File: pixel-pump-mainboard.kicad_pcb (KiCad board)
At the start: 4 copper layers, 68 x 67.3 mm, 130 parts, among them J1 JST NC Valve, J10 BM10B-SRSS-TB(LF)(SN), J11 UART/SWD DNP, J12 TYPE-C-31-M-12, J2 JST NO Valve, J3 6P4C, J4 JST 3 Way Valve, J5 Jack-DC 12V, J6 Power Sw, J7 EXP1, J8 EXP2, J9 BM04B-SRSS-TBT(LF)(SN), Q1 BSS138, Q2 BSS138, Q3 BSS138, Q4 STN4NF20L, Q5 BSS138, SW1 BOOTSEL, U1 LD1117S33TR, U2 TPS62112RSAR, U3 W25Q128JVS, U4 RP2040, Y1 ABMM2-12.000MHZ-E2-T

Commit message: Add robins logo
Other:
- board text added: "REV 7"
- board text removed: "Rev 7"
- board text removed: "by Robin Reiter Hergatz, DE Aug 2022"

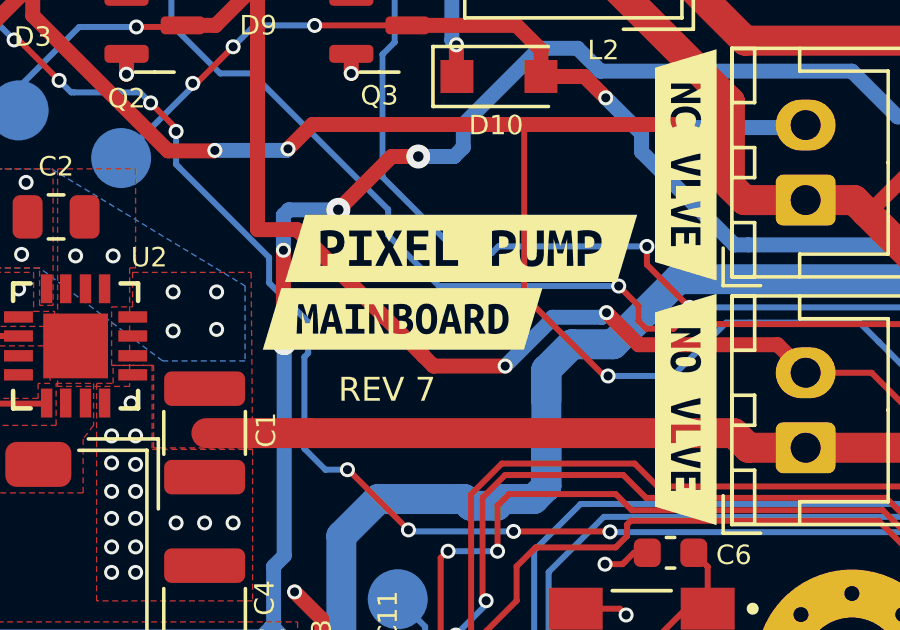
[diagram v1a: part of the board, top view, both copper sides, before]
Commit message: Change appearance of labels
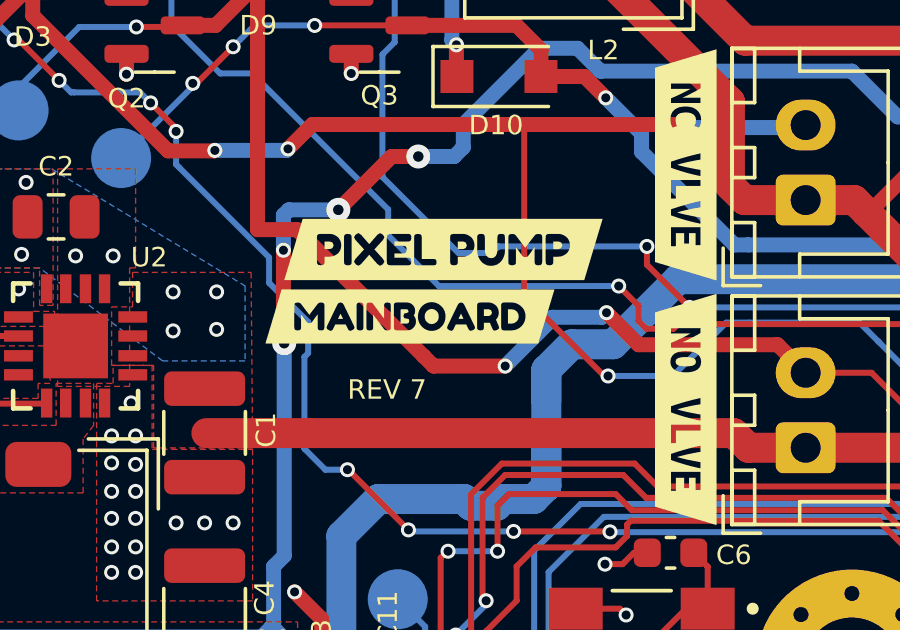
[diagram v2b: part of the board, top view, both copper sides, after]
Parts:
- removed kibuzzard-61080AF0: G***, kibuzzard-61080AF0
- removed kibuzzard-61080B06: G***, kibuzzard-61080B06
- added kibuzzard-62EBC211: G***, kibuzzard-62EBC211, F.Cu at (85.3, 115.6)
- added kibuzzard-62EBC230: G***, kibuzzard-62EBC230, F.Cu at (86.5, 113.4)

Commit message: Change appearance of labels (again)
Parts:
- moved kibuzzard-62EBC211 0.18 mm to (85.5, 115.5)
- moved kibuzzard-62EBC230 0.18 mm to (86.6, 113.3)
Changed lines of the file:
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@@
   )
   (footprint "kibuzzard-62EBC230" (layer "F.Cu")
-    (at 86.4616 113.3856)
+    (at 86.614 113.284)
     (descr "Converted using: scripting")
     (tags "svg2mod")
@@
   )
   (footprint "kibuzzard-62EBC211" (layer "F.Cu")
-    (at 85.344 115.6208)
+    (at 85.4964 115.5192)
     (descr "Converted using: scripting")
     (tags "svg2mod")
@@
   (gr_arc (start 129.699998 139.450136) (mid 130.567849 136.355905) (end 132.918238 134.164307) (layer "Edge.Cuts") (width 0.2))
   (gr_line (start 70.5 139.450136) (end 70.5 152.434856) (layer "Edge.Cuts") (width 0.2))
-  (gr_text "REV 7" (at 84.582 118.0592) (layer "F.SilkS")
+  (gr_text "REV 7" (at 84.8868 117.4496) (layer "F.SilkS")
     (effects (font (size 0.65 0.65) (thickness 0.13)))
   )

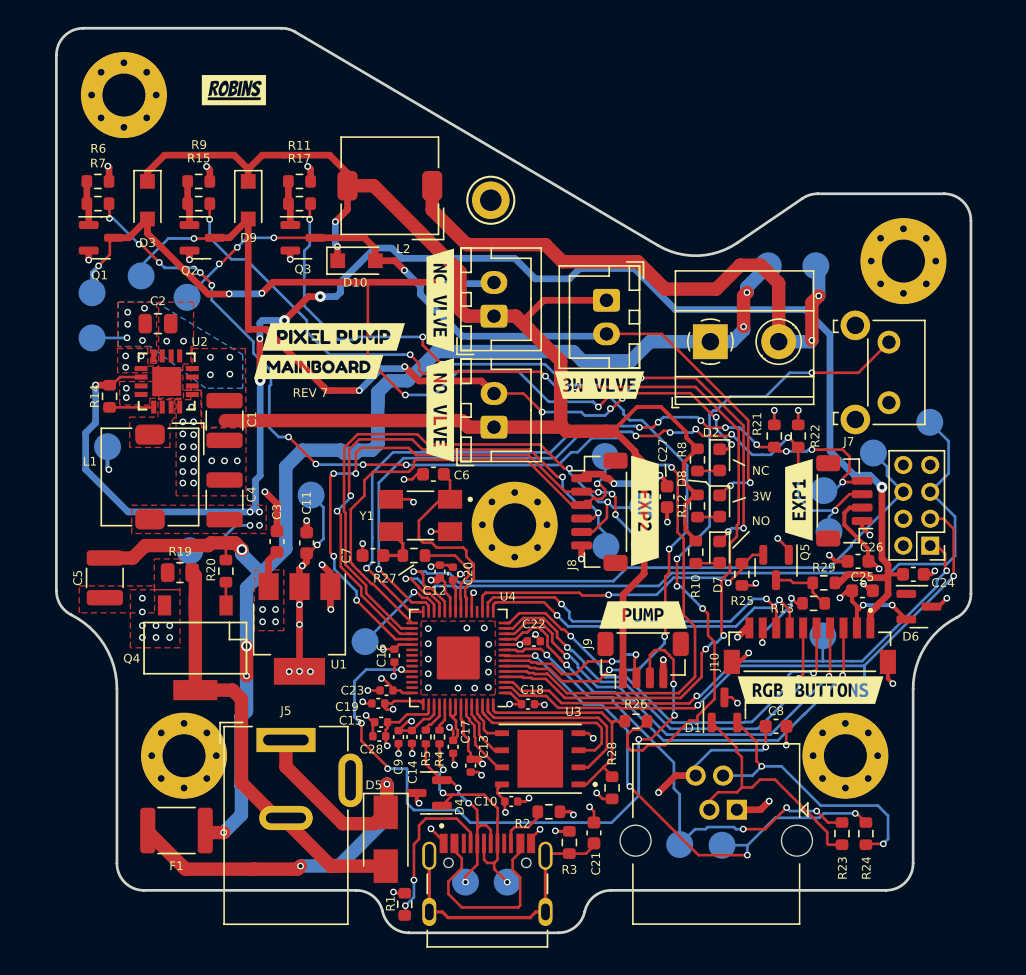
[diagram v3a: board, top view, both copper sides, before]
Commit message: Add fiducials and fix THT parts to be SMD
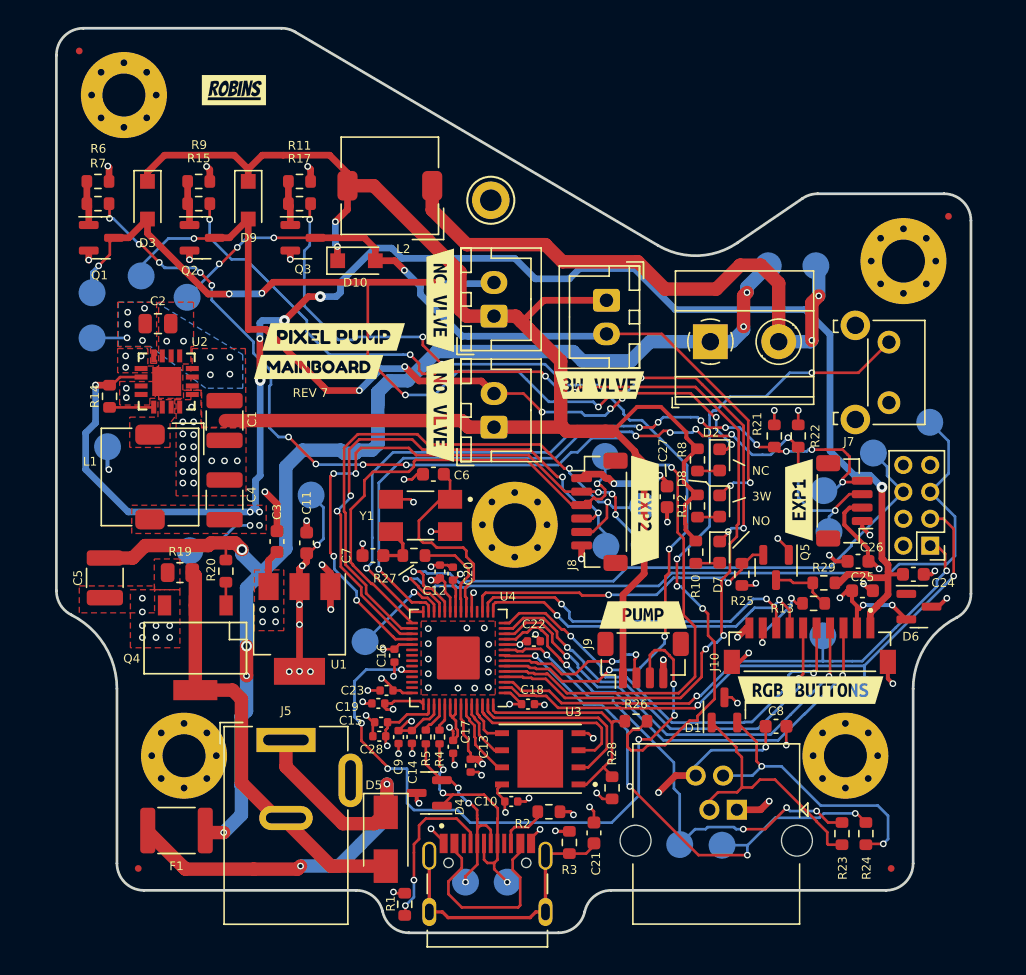
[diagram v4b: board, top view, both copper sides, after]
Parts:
- added FID1: Fiducial, Fiducial:Fiducial_0.5mm_Mask1mm, F.Cu at (72.1, 152.8)
- added FID2: Fiducial, Fiducial:Fiducial_0.5mm_Mask1mm, F.Cu at (132.3, 104.3)
- added FID3: Fiducial, Fiducial:Fiducial_0.5mm_Mask1mm, F.Cu at (67.7, 92.0)
- added FID4: Fiducial, Fiducial:Fiducial_0.5mm_Mask1mm, F.Cu at (128.1, 152.8)
- U3: value W25Q128JVS -> W25Q128JVPIQ
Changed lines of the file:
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@@
     )
   )
+  (footprint "Fiducial:Fiducial_0.5mm_Mask1mm" (layer "F.Cu")
+    (at 128.0668 152.8064)
+    (descr "Circular Fiducial, 0.5mm bare copper, 1mm soldermask opening (Level C)")
+    (tags "fiducial")
+    (property "Sheetfile" "pixel-pump-mainboard.kicad_sch")
+    (property "Sheetname" "")
+    (attr smd)
+    (fp_text reference "FID4" (at 0 -1.5) (layer "F.SilkS") hide
+      (effects (font (size 1 1) (thickness 0.15)))
+    )
+    (fp_text value "Fiducial" (at 0 1.5) (layer "F.Fab")
+      (effects (font (size 1 1) (thickness 0.15)))
+    )
+    (fp_text user "${REFERENCE}" (at 0 0) (layer "F.Fab")
+      (effects (font (size 0.2 0.2) (thickness 0.04)))
+    )
+    (fp_circle (center 0 0) (end 0.75 0) (layer "F.CrtYd") (width 0.05) (fill none))
+    (fp_circle (center 0 0) (end 0.5 0) (layer "F.Fab") (width 0.1) (fill none))
+    (pad "" smd circle (at 0 0) (size 0.5 0.5) (layers "F.Cu" "F.Mask")
+      (solder_mask_margin 0.25) (clearance 0.25))
+  )
   (footprint "Resistor_SMD:R_0603_1608Metric" (layer "F.Cu")
     (at 84.074 101.724)
@@
     (property "Sheetfile" "pixel-pump-mainboard.kicad_sch")
     (property "Sheetname" "")
-    (attr through_hole)
+    (attr smd)
     (fp_text reference "Q4" (at 4.727 -3.9516) (layer "F.SilkS")
       (effects (font (size 0.65 0.65) (thickness 0.13)))
@@
     (pad "1" thru_hole circle locked (at 1.697056 1.697056) (size 0.8 0.8) (drill 0.5) (layers *.Cu *.Mask))
   )
+  (footprint "Fiducial:Fiducial_0.5mm_Mask1mm" (layer "F.Cu")
+    (at 132.328 104.3178)
+    (descr "Circular Fiducial, 0.5mm bare copper, 1mm soldermask opening (Level C)")
+    (tags "fiducial")
+    (property "Sheetfile" "pixel-pump-mainboard.kicad_sch")
+    (property "Sheetname" "")
+    (attr smd)
+    (fp_text reference "FID2" (at 0 -1.5) (layer "F.SilkS") hide
+      (effects (font (size 1 1) (thickness 0.15)))
+    )
+    (fp_text value "Fiducial" (at 0 1.5) (layer "F.Fab")
+      (effects (font (size 1 1) (thickness 0.15)))
+    )
+    (fp_text user "${REFERENCE}" (at 0 0) (layer "F.Fab")
+      (effects (font (size 0.2 0.2) (thickness 0.04)))
+    )
+    (fp_circle (center 0 0) (end 0.75 0) (layer "F.CrtYd") (width 0.05) (fill none))
+    (fp_circle (center 0 0) (end 0.5 0) (layer "F.Fab") (width 0.1) (fill none))
+    (pad "" smd circle (at 0 0) (size 0.5 0.5) (layers "F.Cu" "F.Mask")
+      (solder_mask_margin 0.25) (clearance 0.25))
+  )
   (footprint "Resistor_SMD:R_0402_1005Metric" (layer "F.Cu")
     (at 93.467 143.03 -90)
@@
     (property "Sheetfile" "pixel-pump-mainboard.kicad_sch")
     (property "Sheetname" "")
-    (attr through_hole)
+    (attr smd)
     (fp_text reference "U2" (at -2.45 2.95) (layer "F.SilkS")
       (effects (font (size 0.65 0.65) (thickness 0.13)))
@@
     (property "Sheetfile" "pixel-pump-mainboard.kicad_sch")
     (property "Sheetname" "")
-    (attr through_hole)
+    (attr smd)
     (fp_text reference "J12" (at 0 -1.7355) (layer "F.SilkS") hide
       (effects (font (size 0.65 0.65) (thickness 0.13)))
@@
     )
   )
+  (footprint "Fiducial:Fiducial_0.5mm_Mask1mm" (layer "F.Cu")
+    (at 72.0852 152.8064)
+    (descr "Circular Fiducial, 0.5mm bare copper, 1mm soldermask opening (Level C)")
+    (tags "fiducial")
+    (property "Sheetfile" "pixel-pump-mainboard.kicad_sch")
+    (property "Sheetname" "")
+    (attr smd)
+    (fp_text reference "FID1" (at 0 -1.5) (layer "F.SilkS") hide
+      (effects (font (size 1 1) (thickness 0.15)))
+    )
+    (fp_text value "Fiducial" (at 0 1.5) (layer "F.Fab")
+      (effects (font (size 1 1) (thickness 0.15)))
+    )
+    (fp_text user "${REFERENCE}" (at 0 0) (layer "F.Fab")
+      (effects (font (size 0.2 0.2) (thickness 0.04)))
+    )
+    (fp_circle (center 0 0) (end 0.75 0) (layer "F.CrtYd") (width 0.05) (fill none))
+    (fp_circle (center 0 0) (end 0.5 0) (layer "F.Fab") (width 0.1) (fill none))
+    (pad "" smd circle (at 0 0) (size 0.5 0.5) (layers "F.Cu" "F.Mask")
+      (solder_mask_margin 0.25) (clearance 0.25))
+  )
   (footprint "Resistor_SMD:R_0603_1608Metric" (layer "F.Cu")
     (at 84.074 103.375)
@@
     (property "Sheetfile" "pixel-pump-mainboard.kicad_sch")
     (property "Sheetname" "")
-    (attr through_hole)
+    (attr smd)
     (fp_text reference "Y1" (at 3.9914 -0.0402) (layer "F.SilkS")
       (effects (font (size 0.65 0.65) (thickness 0.13)))
@@
   (footprint "W25Q128JVPIQ TR:SON127P500X600X80-9N" (layer "F.Cu")
     (at 101.976 144.653 180)
-    (property "MPN" "W25Q128JVS")
+    (property "MPN" "W25Q128JVPIQ")
     (property "Sheetfile" "pixel-pump-mainboard.kicad_sch")
     (property "Sheetname" "")
-    (attr through_hole)
+    (attr smd)
     (fp_text reference "U3" (at -2.4688 3.4798 180) (layer "F.SilkS")
       (effects (font (size 0.65 0.65) (thickness 0.13)))
     )
-    (fp_text value "W25Q128JVS" (at 8.61 3.362 180) (layer "F.Fab")
+    (fp_text value "W25Q128JVPIQ" (at 8.61 3.362 180) (layer "F.Fab")
       (effects (font (size 1 1) (thickness 0.015)))
     )
@@
     )
   )
+  (footprint "Fiducial:Fiducial_0.5mm_Mask1mm" (layer "F.Cu")
+    (at 67.697 92.0242)
+    (descr "Circular Fiducial, 0.5mm bare copper, 1mm soldermask opening (Level C)")
+    (tags "fiducial")
+    (property "Sheetfile" "pixel-pump-mainboard.kicad_sch")
+    (property "Sheetname" "")
+    (attr smd)
+    (fp_text reference "FID3" (at 0 -1.5) (layer "F.SilkS") hide
+      (effects (font (size 1 1) (thickness 0.15)))
+    )
+    (fp_text value "Fiducial" (at 0 1.5) (layer "F.Fab")
+      (effects (font (size 1 1) (thickness 0.15)))
+    )
+    (fp_text user "${REFERENCE}" (at 0 0) (layer "F.Fab")
+      (effects (font (size 0.2 0.2) (thickness 0.04)))
+    )
+    (fp_circle (center 0 0) (end 0.75 0) (layer "F.CrtYd") (width 0.05) (fill none))
+    (fp_circle (center 0 0) (end 0.5 0) (layer "F.Fab") (width 0.1) (fill none))
+    (pad "" smd circle (at 0 0) (size 0.5 0.5) (layers "F.Cu" "F.Mask")
+      (solder_mask_margin 0.25) (clearance 0.25))
+  )
   (footprint "TerminalBlock_Phoenix:TerminalBlock_Phoenix_MKDS-1,5-2-5.08_1x02_P5.08mm_Horizontal" (layer "F.Cu")
     (at 114.6252 113.6398)
@@
     (property "Sheetfile" "pixel-pump-mainboard.kicad_sch")
     (property "Sheetname" "")
-    (attr through_hole)
+    (attr smd)
     (fp_text reference "J10" (at 7.0866 -2.5428 90) (layer "F.SilkS")
       (effects (font (size 0.65 0.65) (thickness 0.13)))
@@
     (connect_pads yes (clearance 0))
     (min_thickness 0.254)
-    (keepout (tracks allowed) (vias allowed) (pads allowed ) (copperpour not_allowed) (footprints allowed))
+    (keepout (tracks allowed) (vias allowed) (pads allowed) (copperpour not_allowed) (footprints allowed))
     (fill (thermal_gap 0.508) (thermal_bridge_width 0.508))
     (polygon

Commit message: Bump rev to 8
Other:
- board text added: "REV 8"
- board text removed: "REV 7"
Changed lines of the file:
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@@
   (gr_arc (start 129.699998 139.450136) (mid 130.567849 136.355905) (end 132.918238 134.164307) (layer "Edge.Cuts") (width 0.2))
   (gr_line (start 70.5 139.450136) (end 70.5 152.434856) (layer "Edge.Cuts") (width 0.2))
-  (gr_text "REV 7" (at 84.8868 117.4496) (layer "F.SilkS")
+  (gr_text "REV 8" (at 84.8868 117.4496) (layer "F.SilkS")
     (effects (font (size 0.65 0.65) (thickness 0.13)))
   )

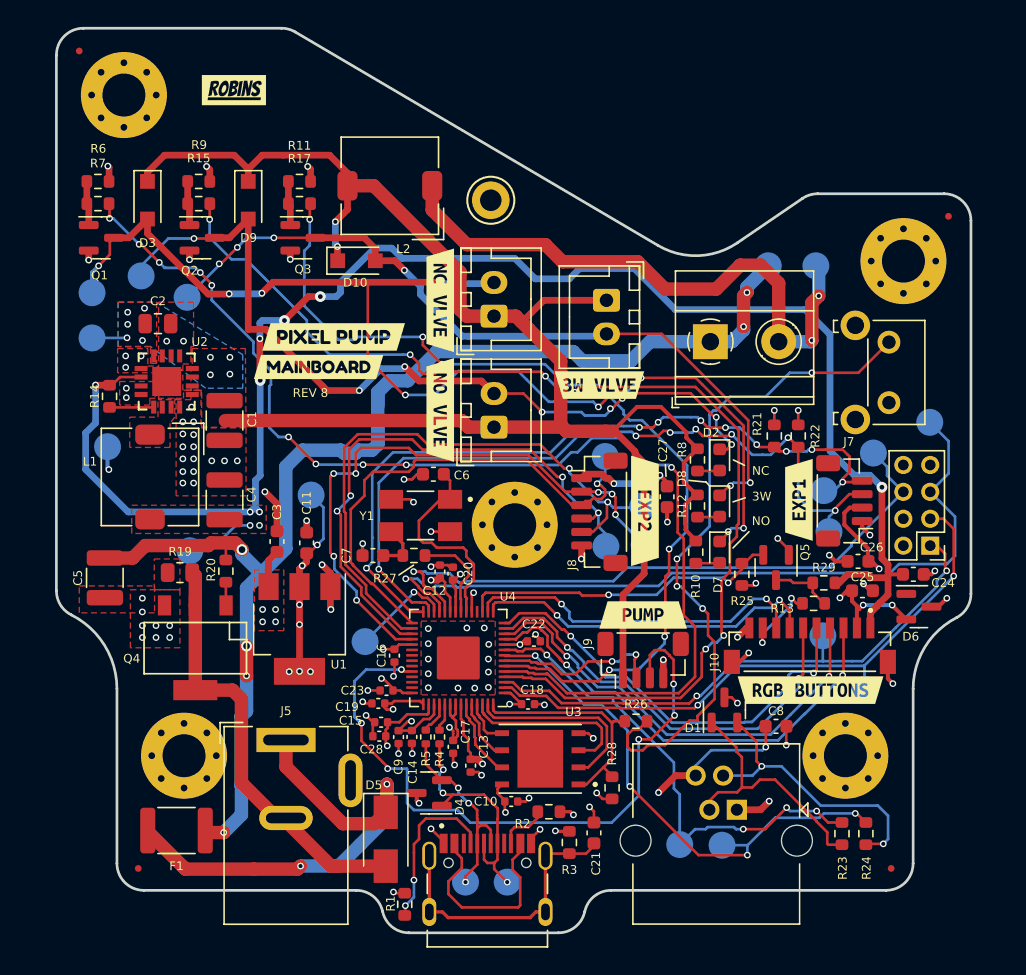
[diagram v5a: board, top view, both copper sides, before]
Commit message: Remove DNP parts from BOM, increase Fiducial to 0.75/1.5mm
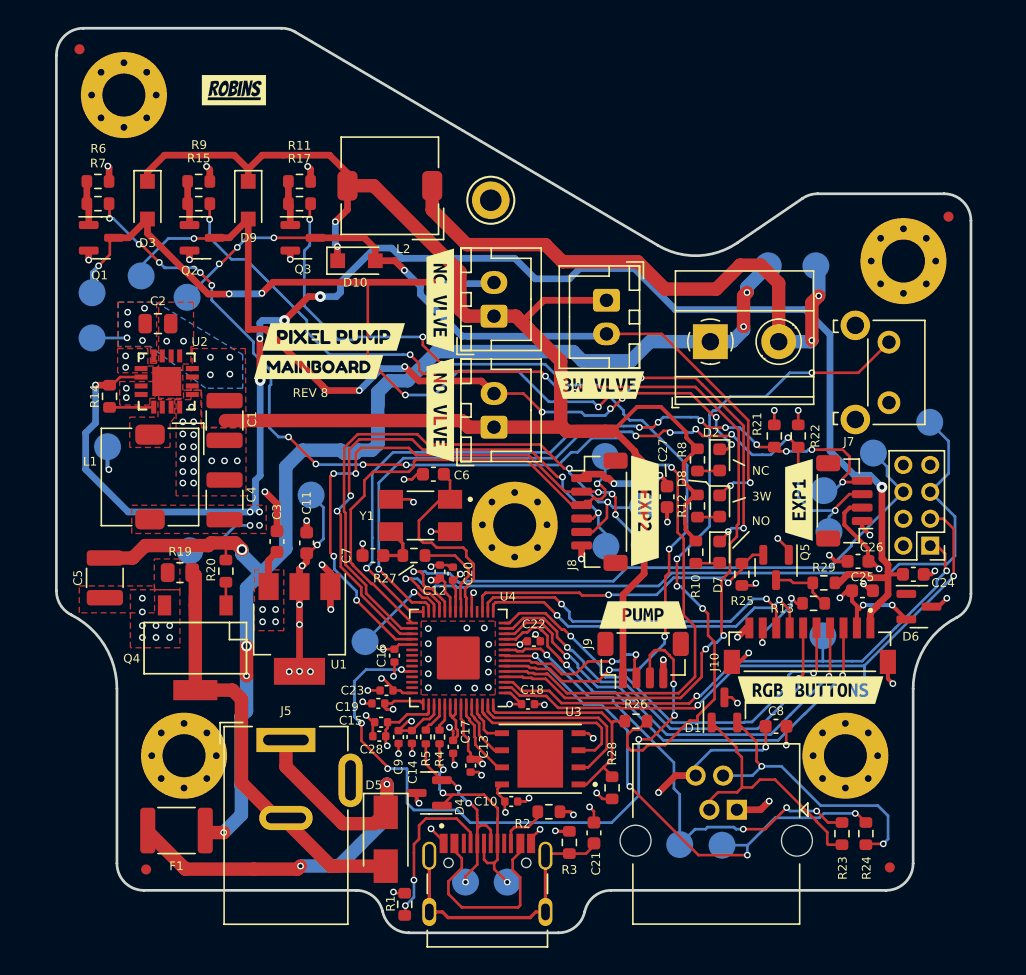
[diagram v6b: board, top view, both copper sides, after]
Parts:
- FID1, FID2, FID3, FID4: footprint Fiducial:Fiducial_0.5mm_Mask1mm -> Fiducial:Fiducial_0.75mm_Mask1.5mm
- moved FID3 65.8 mm to (132.3, 104.3)
- moved FID2 65.8 mm to (67.7, 91.9)
- moved FID1 0.59 mm to (72.7, 152.9)
- moved FID4 0.13 mm to (128.0, 152.7)
